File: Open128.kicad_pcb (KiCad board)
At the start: 2 copper layers, 406.6 x 253.4 mm, 370 parts, among them CN1 Expansion bus, CN10 RGBI 9-pin DIN, CN11 Power DIN connector, CN12 6 pin post, CN13 Power LED, CN2 Cassette, CN20 TA11, CN3 Port1 Male DB9, CN4 Port2 Male DB9, CN5 Conn_01x25, CN6 DIN6 Male, CN7 7 pin post, CN8 8 pin DIN, CN9 User Port, J1 C:PAL / O:NTSC, J2 Close to enable CAS latch, J3 Close to enable CAS latch, J4 128/256k, J6 128/256k, J7 SolderJumper_3_Bridged12, M1 RF_Modulator, Q1 2SC1815, Q2 2SC1815, Q3 2SD880, Q4 2SC1815, Q5 2SC1815, Q6 2SC1815, SW1 Power switch, SW2 Reset Switch, SW3 Disk Reset, U1 6526A, U10 Z80, U11 8721, U12 74LS373, U13 74LS244, U14 74LS257, U15 74LS257, U16 74LS14, U17 74LS373, U18 2364, U19 2016, U2 4066, U20 4066, U21 8564, U22 8563, U23 4464, U24 74LS244, U25 4464, U26 74LS257, U27 LM556, U28 8701, U29 7406, U3 74LS138, U30 7406, U31 74LS00, U32 23128, U33 23128, U34 23128, U35 318020-03, U36 23256, U37 7406, U38 4164, U39 4164, U4 6526A, U40 4164, U41 4164, U42 4164, U43 4164, U44 4164, U45 4164, U46 4164, U47 4164, U48 4164, U49 4164, U5 6581, U50 4164, U51 4164, U52 4164, U53 4164, U54 74LS32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

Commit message: Fix R47/R101
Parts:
- added R47: 1k, Open128:R_Axial_DIN0309_L9.0mm_D2.5mm_P12.70mm_Horizontal, F.Cu at (266.7, 90.2)
- renumbered R47 to R101
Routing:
- net Net-(FB18-Pad2): track 138.7 -> 138.9 mm, vias 5 -> 4
- net +5V: vias 93 -> 92
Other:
- board text added: "Open128 rev.2 202106"
- board text removed: "Open128 rev.1 202103"

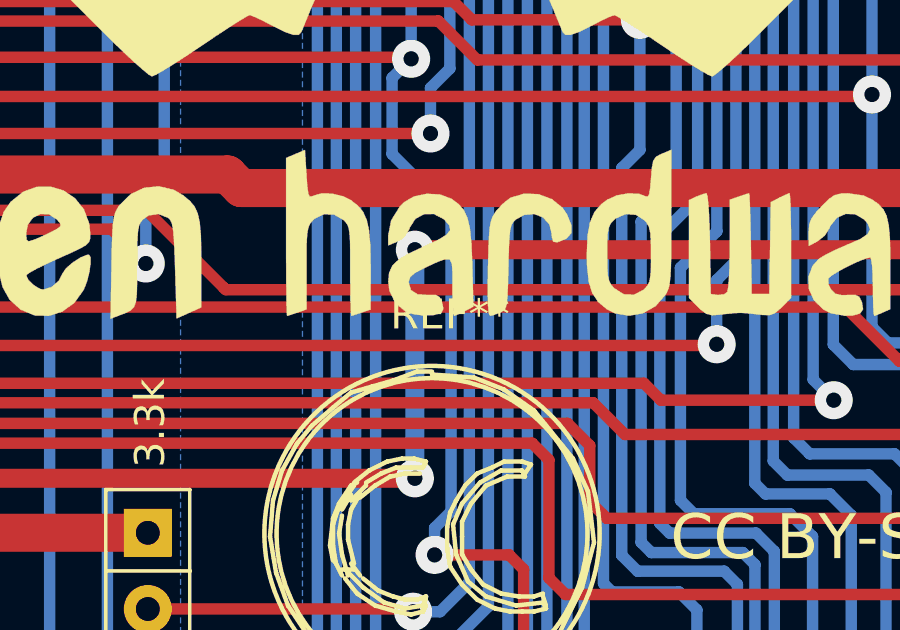
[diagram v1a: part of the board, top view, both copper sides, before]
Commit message: Clean up schematic
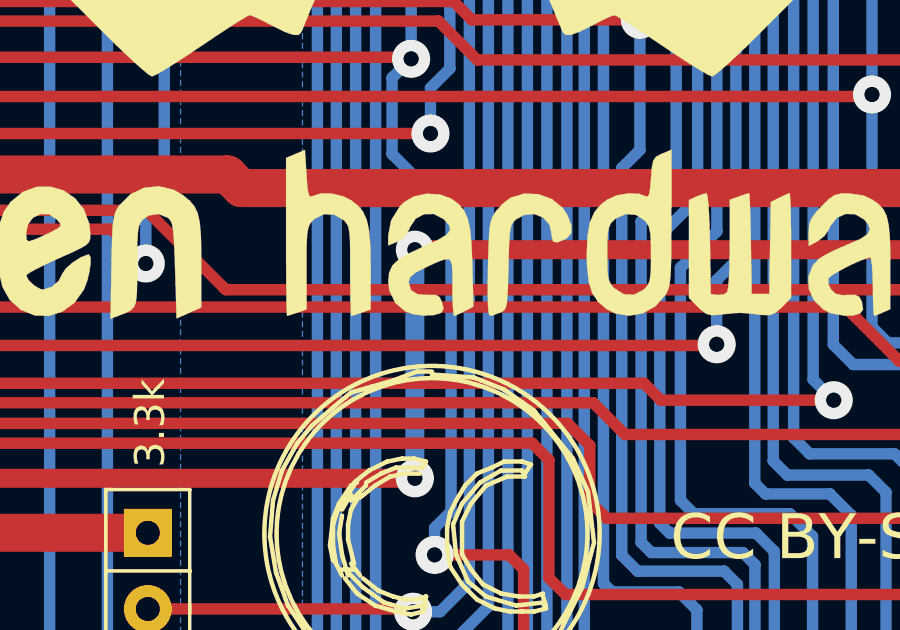
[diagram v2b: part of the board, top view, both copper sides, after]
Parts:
- LOGO1: renamed from REF**; value OSHW-Logo2_48.7x40mm_SilkScreen -> OSHW logo
- LOGO2: renamed from REF**; value KiCad-Logo2_8mm_SilkScreen -> KiCad logo
- LOGO3: renamed from G***; value LOGO -> C128 logo
- LOGO4: renamed from REF**; value Symbol_CreativeCommons_SilkScreenTop_Type2_Big -> Creative Commons
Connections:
- net /AEC renamed AEC
- net /Address Multiplexing/MUX renamed MUX
- net /Address Multiplexing/VA14 renamed VA14
- net /Address Multiplexing/VA15 renamed VA15
- net /Address Multiplexing/VA6 renamed VA6
- net /Address Multiplexing/VA7 renamed VA7
- net /Address Multiplexing/~AEC renamed ~AEC
- net /Address Multiplexing/~RAS renamed ~RAS
- net /BA renamed BA
- net /CPU 8502/2MHZ renamed 2MHZ
- net /CPU 8502/8052_RW renamed Net-(R27-Pad2)
- net /CPU 8502/CAPLK renamed CAPSLK
- net /CPU 8502/DMA renamed ~DMA
- net /CPU 8502/F_R~W renamed F_R~W
- net /CPU 8502/Z80_RW renamed Z80_R~W
- net /CPU 8502/~BUSACK renamed ~BUSACK
- net /CPU 8502/~MMU_Z80EN renamed ~MMU_Z80EN
- net /CPU 8502/~NMI renamed ~NMI
- net /CPU Z80/D1MHZ renamed D1MHZ
- net /CPU Z80/GAEC renamed GAEC
- net /CPU Z80/~Z80IO renamed ~Z80_IO
- net /CPU Z80/ΦZ80 renamed ΦZ80
- net /Clock/TOD renamed TOD
- net /Clock/~ϕDOT renamed ~ΦDOT
- net /DRAM/~CAS renamed ~CAS
- net /DRAM/~DWE renamed ~DWE
- net /DRAM/~GCAS0 renamed ~GCAS0
- net /DRAM/~GCAS1 renamed ~GCAS1
- net /Expansion Port/1MHZ renamed 1MHZ
- net /Expansion Port/~EXROM renamed ~EXROM
- net /Expansion Port/~GAME renamed ~GAME
- net /I/O/128_64 renamed 128_64
- net /I/O/4080 renamed 40_80
- net /I/O/POTX renamed POTX
- net /I/O/POTY renamed POTY
- net /I/O/~DRESET renamed ~DRESET
- net /I/O/~VA14 renamed ~VA14
- net /Memory Management/CLRBNK renamed CLRBNK
- net /Memory Management/FSDIR renamed ~FSDIR
- net /Memory Management/M1 renamed ~M1
- net /Memory Management/~BUSACK renamed ~PLA_Z80EN
- net /Memory Management/~GWE renamed ~GWE
- net /Memory Management/~IOACC renamed ~IOACC
- net /R~W renamed R~W
- net /Sound/AUDIO_OUT renamed AUDIO_OUT
- net /Sound/EXT_AUDIO renamed EXT_AUDIO
- net /VIC/K0 renamed K0
- net /VIC/K1 renamed K1
- net /VIC/K2 renamed K2
- net /VIC/~LIGHTPEN renamed ~LP
- net /VIC/ΦCOLOR renamed ΦCOLOR
- net /VIC/ΦDOT renamed ΦDOT
- net /~IRQ renamed ~IRQ
